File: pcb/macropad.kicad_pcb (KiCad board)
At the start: 2 copper layers, 94.2 x 90 mm, 40 parts, among them SW1 RotaryEncoder, SW10 SW_Push, SW2 SW_Push, SW3 SW_Push, SW4 SW_Push, SW5 SW_Push, SW6 SW_Push, SW7 SW_Push, SW8 SW_Push, SW9 SW_Push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

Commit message: added drawings and mounting holes
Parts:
- added G***: LOGO, LOGO, F.Cu at (124.0, 87.8)
- added G***: LOGO, LOGO, F.Cu at (179.4, 59.4)
- added G***: LOGO, LOGO, F.Cu at (122.5, 134.0)
- added G***: LOGO, LOGO, B.Cu at (164.4, 74.4)
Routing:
- net EC11_S2: track 43.0 -> 46.4 mm

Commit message: added gerbers
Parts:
- added REF**: MountingHole_3.2mm_M3, MountingHole:MountingHole_3.2mm_M3, F.Cu at (136.0, 71.0)
- added REF**: MountingHole_3.2mm_M3, MountingHole:MountingHole_3.2mm_M3, F.Cu at (111.5, 139.0)
- added REF**: MountingHole_3.2mm_M3, MountingHole:MountingHole_3.2mm_M3, F.Cu at (198.0, 57.0)
- moved G*** 3.95 mm to (175.5, 60.0)
- moved G*** 3.00 mm to (125.5, 134.0)

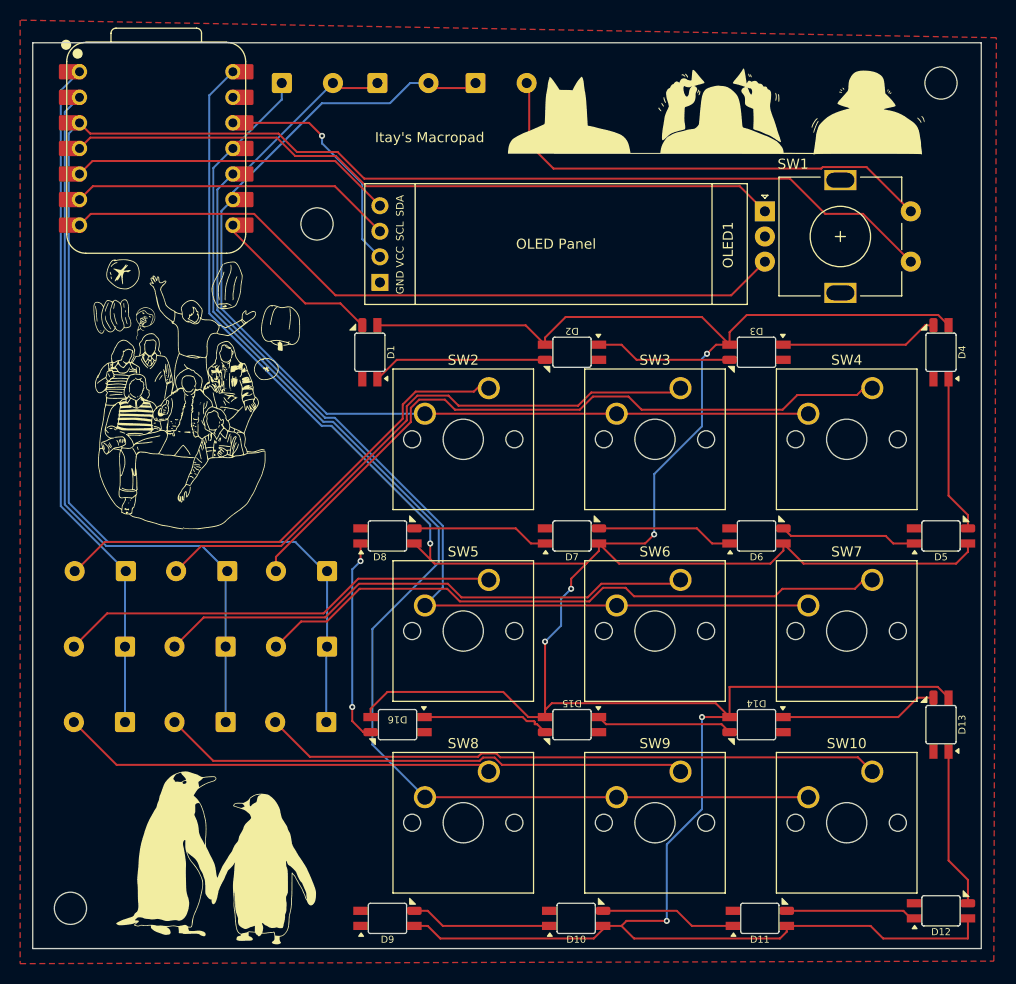
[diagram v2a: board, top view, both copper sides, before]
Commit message: switched to the correct diode footprint
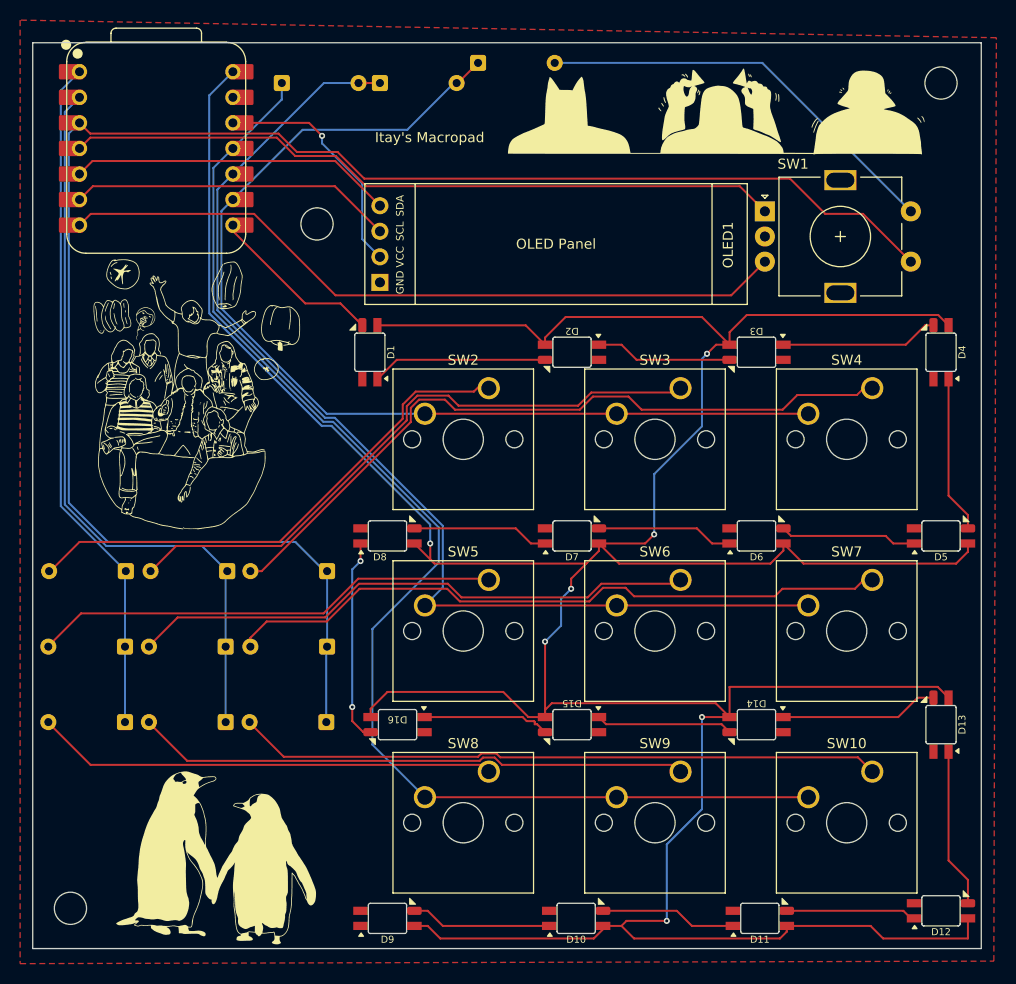
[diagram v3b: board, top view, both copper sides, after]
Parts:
- D17, D18, D19, D20, D21, D22, D23, D24, D25, D26, D27, D28: footprint Diode_THT:D_T-1_P5.08mm_Horizontal -> Diode_THT:D_DO-35_SOD27_P7.62mm_Horizontal
- moved D17 2.02 mm to (152.0, 55.0)
- moved D18 0.25 mm to (142.2, 57.0)
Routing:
- net EC11_S2: track 46.4 -> 41.5 mm
- net Net-(D23-A): track 62.9 -> 66.0 mm
- net Net-(D22-A): track 49.1 -> 51.7 mm
- net Net-(D24-A): track 53.6 -> 56.2 mm
- net Net-(D28-A): track 42.3 -> 44.9 mm
- net Net-(D25-A): track 43.9 -> 46.5 mm
- net Net-(D27-A): track 51.6 -> 54.2 mm
- net Net-(D26-A): track 61.6 -> 64.2 mm
- net Net-(D21-A): track 58.7 -> 61.2 mm
- net Net-(D20-A): track 69.5 -> 71.2 mm
- net COL2: track 102.8 -> 103.9 mm
- net COL1: track 109.5 -> 110.5 mm
